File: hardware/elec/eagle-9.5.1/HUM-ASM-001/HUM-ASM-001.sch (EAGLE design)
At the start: 61 parts, among them J1 B2B-XH-AM(LF)(SN), J2 75869-131LF, J22 75869-131LF, J23 75869-131LF, K1 7-1393239-7, K2 7-1393239-7, Q1 IRLB8721PBF, Q2 IRLB8721PBF, U1 MCP23017-E/SP

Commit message: * Fixed crash / recovery inconsistency * Pre silk screen clean up
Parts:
- J10, J11: device MG-Eagle_v1:CON_HEADER_1X4NO_SILK_ALL_ROUND -> MG-Eagle_v1:CON_HEADER_1X4PTH
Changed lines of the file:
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@@
 <part name="U$26" library="MG-Eagle_v1" deviceset="V48" device=""/>
 <part name="U$27" library="MG-Eagle_v1" deviceset="V5.0" device=""/>
-<part name="J10" library="MG-Eagle_v1" deviceset="CON_HEADER_1X4" device="NO_SILK_ALL_ROUND"/>
-<part name="J11" library="MG-Eagle_v1" deviceset="CON_HEADER_1X4" device="NO_SILK_ALL_ROUND"/>
+<part name="J10" library="MG-Eagle_v1" deviceset="CON_HEADER_1X4" device="PTH"/>
+<part name="J11" library="MG-Eagle_v1" deviceset="CON_HEADER_1X4" device="PTH"/>
 <part name="J12" library="MG-Eagle_v1" deviceset="CON_HEADER_1X4" device="NO_SILK_ALL_ROUND"/>
 <part name="U$28" library="MG-Eagle_v1" deviceset="V0_GND" device=""/>

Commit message: * Normalized Text for Names and Values
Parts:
- removed J26, J27: (no value), MG-Eagle_v1:CON_HEADER_1X1-QC_TAB_121786-1
- removed JP13, JP14: CON_JUMPER_PAD-2-NC_BY_TRACE, MG-Eagle_v1:CON_JUMPER_PAD-2-NC_BY_TRACE
- added J5: (no value), MG-Eagle_v1:CON_HEADER_1X7NO_SILK
- added J6: (no value), MG-Eagle_v1:CON_HEADER_1X1-QC_TAB_121786-1
- added JP1, JP2: CON_JUMPER_PAD-2-NC_BY_TRACE, MG-Eagle_v1:CON_JUMPER_PAD-2-NC_BY_TRACE
- added LED2: 3mm Green, MG-Eagle_v1:LED_THT-3MM
- added R11: 100, MG-Eagle_v1:RES_RESISTOR-PTH-1/4W
- ASM-1: value Feather Bluefruit 32u4 -> (none); device MG-Eagle_v1:ASM_ADAFRUIT_FEATHER_BLUEFRUIT -> MG-Eagle_v1:ASM_ADAFRUIT_MAX98306_AMP
- ASM-2: device MG-Eagle_v1:ASM_ADAFRUIT_SOUND_FX_BOARD -> MG-Eagle_v1:ASM_ADAFRUIT_INA169
- ASM-3: value (none) -> Feather Bluefruit 32u4; device MG-Eagle_v1:ASM_ADAFRUIT_MAX98306_AMP -> MG-Eagle_v1:ASM_ADAFRUIT_FEATHER_BLUEFRUIT
- ASM-4: device MG-Eagle_v1:ASM_ADAFRUIT_INA169 -> MG-Eagle_v1:ASM_ADAFRUIT_SOUND_FX_BOARD
- J1: value B2B-XH-AM(LF)(SN) -> (none); device MG-Eagle_v1:CON_JST_2-PIN_B2B-XH-AM -> MG-Eagle_v1:CON_HEADER_1X6NO_SILK_FEMALE_PTH
- J10: device MG-Eagle_v1:CON_HEADER_1X4PTH -> MG-Eagle_v1:CON_HEADER_1X31X03_NO_SILK
- J11: device MG-Eagle_v1:CON_HEADER_1X4PTH -> MG-Eagle_v1:CON_HEADER_1X1-QC_TAB_121786-1
- J12: device MG-Eagle_v1:CON_HEADER_1X4NO_SILK_ALL_ROUND -> MG-Eagle_v1:CON_HEADER_1X12_NO_SILK
- J13: device MG-Eagle_v1:CON_HEADER_1X31X03_NO_SILK -> MG-Eagle_v1:CON_HEADER_1X16-1X16_NO_SILK
- J14: device MG-Eagle_v1:CON_HEADER_1X31X03_NO_SILK -> MG-Eagle_v1:CON_HEADER_1X21X02_NO_SILK
- J15, J16: device MG-Eagle_v1:CON_HEADER_1X21X02_NO_SILK -> MG-Eagle_v1:CON_HEADER_1X14
- J17, J18: device MG-Eagle_v1:CON_HEADER_1X1-QC_TAB_121786-1 -> MG-Eagle_v1:CON_HEADER_1X4PTH
- J19: device MG-Eagle_v1:CON_HEADER_1X5NO_SILK -> MG-Eagle_v1:CON_HEADER_1X21X02_NO_SILK
- J20: value (none) -> 75869-131LF; device MG-Eagle_v1:CON_HEADER_1X21X02_NO_SILK -> MG-Eagle_v1:CON_HEADER_2X3SHROUD
- J21: value (none) -> 75869-131LF; device MG-Eagle_v1:CON_HEADER_1X6NO_SILK_FEMALE_PTH -> MG-Eagle_v1:CON_HEADER_2X3SHROUD
- J22: value 75869-131LF -> (none); device MG-Eagle_v1:CON_HEADER_2X3SHROUD -> MG-Eagle_v1:CON_HEADER_1X4NO_SILK_ALL_ROUND
- J23: value 75869-131LF -> (none); device MG-Eagle_v1:CON_HEADER_2X3SHROUD -> MG-Eagle_v1:CON_HEADER_1X31X03_NO_SILK
- J3: value (none) -> B2B-XH-AM(LF)(SN); device MG-Eagle_v1:CON_HEADER_1X16-1X16_NO_SILK -> MG-Eagle_v1:CON_JST_2-PIN_B2B-XH-AM
- J4: device MG-Eagle_v1:CON_HEADER_1X12_NO_SILK -> MG-Eagle_v1:CON_HEADER_1X21X02_NO_SILK
- J7: device MG-Eagle_v1:CON_HEADER_1X14 -> MG-Eagle_v1:CON_HEADER_1X5NO_SILK
- J8: device MG-Eagle_v1:CON_HEADER_1X14 -> MG-Eagle_v1:CON_HEADER_1X1-QC_TAB_121786-1
- J9: device MG-Eagle_v1:CON_HEADER_1X7NO_SILK -> MG-Eagle_v1:CON_HEADER_1X1-QC_TAB_121786-1
- R1: value 1k -> 10k
- R2: value 100 -> 4k, 1%
- R3: value 10k -> 220
- R5: value 220 -> 100
- R6: value 4k, 1% -> 100
- R7: value 10k -> 1k
- R9: value 100 -> 10k
- VRG-1: value NID100-5 -> LM317; device MG-Eagle_v1:VRG_NID100 -> MG-Eagle_v1:VRG_LM317_TO-220_VERTICAL
- VRG-2: value LM317 -> NID100-5; device MG-Eagle_v1:VRG_LM317_TO-220_VERTICAL -> MG-Eagle_v1:VRG_NID100
- renumbered JP10 to JP4, JP11 to JP5, JP12 to JP6, JP9 to JP3, THM-2 to THM-1
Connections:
- new net N$19: LED2.A, R11.P1
- net !AMP-SHDN: now also ASM-1.!SHTDWN, ASM-3.D10, J12.7, J5.5, R7.P2; no longer ASM-1.D10, ASM-3.!SHTDWN, J4.7, J9.5, R1.P2
- net 24V: now also J3.1, J4.P1, R3.P2, VRG-1.VOUT; no longer J1.1, J20.P1, R5.P2, VRG-2.VOUT
- net 3V: now also ASM-3.3V, J13.2; no longer ASM-1.3V, J3.2
- net 48V: now also J10.P2, J22.3, J22.4, J23.P2, J9.1, VRG-1.VIN, VRG-2.VIN@10, VRG-2.VIN@9; no longer J12.3, J12.4, J13.P2, J14.P2, J26.1, VRG-1.VIN@10, VRG-1.VIN@9, VRG-2.VIN
- net 5V: now also ASM-1.VCC, ASM-2.VCC, ASM-3.USB/VBUS, ASM-4.VIN, J12.3, J14.P1, J15.1, J17.1, J17.2, J17.3, J17.4, J19.P1, J20.1, J20.2, J21.1, J21.2, J5.7, J7.5, LED2.C, VRG-2.VOUT@1, VRG-2.VOUT@2, VRG-2.VOUT@3, VRG-2.VOUT@4; no longer ASM-1.USB/VBUS, ASM-2.VIN, ASM-3.VCC, ASM-4.VCC, J10.1, J10.2, J10.3, J10.4, J15.P1, J16.P1, J19.5, J22.1, J22.2, J23.1, J23.2, J4.3, J8.1, J9.7, VRG-1.VOUT@1, VRG-1.VOUT@2, VRG-1.VOUT@3, VRG-1.VOUT@4
- net ADJ: now also R2.P2, R3.P1, VRG-1.ADJ; no longer R5.P1, R6.P2, VRG-2.ADJ
- net CRNT-MON: now also ASM-2.OUT, ASM-3.A0, J13.5, J7.1; no longer ASM-1.A0, ASM-4.OUT, J19.1, J3.5
- net DFU: now also ASM-3.DFU, J13.16; no longer ASM-1.DFU, J3.16
- net ENCODER-A: now also ASM-3.RX0, J13.14; no longer ASM-1.RX0, J3.14
- net ENCODER-B: now also ASM-3.TX1, J13.15, JP7.1; no longer ASM-1.TX1, J3.15, JP13.1
- net ENCODER-SW: now also ASM-3.A5, J13.10; no longer ASM-1.A5, J3.10
- net FAN-CTRL: now also ASM-3.D6, J12.9, R4.P1; no longer ASM-1.D6, J4.9, R8.P1
- net GND: now also ASM-1.GND, ASM-2.GND, ASM-3.GND@4, ASM-4.GND@14, ASM-4.GND@27, ASM-4.L-GND, ASM-4.R-GND, J13.4, J15.11, J15.14, J15.2, J16.14, J18.2, J18.3, J18.4, J20.5, J20.6, J21.5, J21.6, J5.6, J7.4, J8.1, JP1.1, JP2.1, R1.P2, R11.P2, R2.P1, R7.P1, R9.P2, VRG-2.GND@5, VRG-2.GND@6, VRG-2.GND@7, VRG-2.GND@8; no longer ASM-1.GND@4, ASM-2.GND@14, ASM-2.GND@27, ASM-2.L-GND, ASM-2.R-GND, ASM-3.GND, ASM-4.GND, J11.2, J11.3, J11.4, J19.4, J22.5, J22.6, J23.5, J23.6, J27.1, J3.4, J7.14, J8.11, J8.14, J8.2, J9.6, JP14.1, JP7.1, R1.P1, R3.P2, R6.P1, R7.P2, VRG-1.GND@5, VRG-1.GND@6, VRG-1.GND@7, VRG-1.GND@8
- net I2C-SCL: now also ASM-3.SCL, J12.11; no longer ASM-1.SCL, J4.11
- net I2C-SDA: now also ASM-3.SDA, J12.12; no longer ASM-1.SDA, J4.12
- net K1-NC: now also J10.P1; no longer J13.P1
- net K2-NC: now also J23.P1; no longer J14.P1
- net LED1-DATA: now also ASM-3.D12, J12.5, R5.P2; no longer ASM-1.D12, J4.5, R9.P2
- net LED2-DATA: now also ASM-3.D11, J12.6, R6.P1; no longer ASM-1.D11, J4.6, R10.P1
- net MIST-CTRL: now also ASM-3.D5, J12.10, R8.P1; no longer ASM-1.D5, J4.10, R2.P1
- net MIST-VIN: now also ASM-2.VIN-, J10.P3, J23.P3, J6.1, J7.3; no longer ASM-4.VIN-, J13.P3, J14.P3, J17.1, J19.3
- net N$1: now also ASM-3.!RESET, J13.1; no longer ASM-1.!RESET, J3.1
- net N$10: now also J14.P2, J19.P2, Q2.D, R10.P1; no longer J15.P2, J16.P2, Q1.D, R4.P1
- net N$11: now also Q2.G, R8.P2, R9.P1; no longer Q1.G, R2.P2, R3.P1
- net N$12: now also J3.2, J4.P2, Q1.D; no longer J1.2, J20.P2, Q2.D
- net N$13: now also R10.P2; no longer R4.P2
- net N$14: now also ASM-1.L-IN, J5.3, JP2.2; no longer ASM-3.L-IN, J9.3, JP7.2
- net N$15: now also ASM-1.R-IN, J5.2, JP1.2; no longer ASM-3.R-IN, J9.2, JP8.2
- net N$16: now also ASM-2.VIN+, J7.2; no longer ASM-4.VIN+, J19.2
- net N$17: now also Q1.G, R1.P1, R4.P2; no longer Q2.G, R7.P1, R8.P2
- net N$18: now also J1.1; no longer J21.1
- net N$2: now also ASM-3.AREF, J13.3; no longer ASM-1.AREF, J3.3
- net N$20: now also ASM-3.D9, J12.8; no longer ASM-1.D9, J4.8
- net N$21: now also J1.2; no longer J21.2
- net N$22: now also J1.3; no longer J21.3
- net N$24: now also ASM-3.D13, J12.4; no longer ASM-1.D13, J4.4
- net N$25: now also ASM-3.EN, J12.2; no longer ASM-1.EN, J4.2
- net N$26: now also ASM-4.ACT, J16.13; no longer ASM-2.ACT, J7.13
- net N$27: now also J22.1, VRG-2.R.C.; no longer J12.1, VRG-1.R.C.
- net N$29: now also J22.2, VRG-2.TRIM; no longer J12.2, VRG-1.TRIM
- net N$30: now also ASM-4.TX, J15.5; no longer ASM-2.TX, J8.5
- net N$31: now also ASM-4.RX, J15.6; no longer ASM-2.RX, J8.6
- net N$38: now also ASM-4.UART/GPIO_SEL, J15.7; no longer ASM-2.UART/GPIO_SEL, J8.7
- net N$39: now also J1.4; no longer J21.4
- net N$40: now also J1.5, JP7.2; no longer J21.5, JP13.2
- net N$41: now also J1.6, JP8.2; no longer J21.6, JP14.2
- net N$42: now also J21.3, J21.4, R6.P2; no longer J23.3, J23.4, R10.P2
- net N$5: now also ASM-3.A1, J13.6; no longer ASM-1.A1, J3.6
- net N$6: now also ASM-3.A2, J13.7; no longer ASM-1.A2, J3.7
- net N$7: now also ASM-3.A3, J13.8; no longer ASM-1.A3, J3.8
- net N$8: now also ASM-3.A4, J13.9; no longer ASM-1.A4, J3.9
- net N$9: now also J20.3, J20.4, R5.P1; no longer J22.3, J22.4, R9.P1
- net SFX-0: now also ASM-4.0, J16.2; no longer ASM-2.0, J7.2
- net SFX-1: now also ASM-4.1, J16.3; no longer ASM-2.1, J7.3
- net SFX-10: now also ASM-4.10, J16.12; no longer ASM-2.10, J7.12
- net SFX-2: now also ASM-4.2, J16.4; no longer ASM-2.2, J7.4
- net SFX-3: now also ASM-4.3, J16.5; no longer ASM-2.3, J7.5
- net SFX-4: now also ASM-4.4, J16.6; no longer ASM-2.4, J7.6
- net SFX-5: now also ASM-4.5, J16.7; no longer ASM-2.5, J7.7
- net SFX-6: now also ASM-4.6, J16.8; no longer ASM-2.6, J7.8
- net SFX-7: now also ASM-4.7, J16.9; no longer ASM-2.7, J7.9
- net SFX-8: now also ASM-4.8, J16.10; no longer ASM-2.8, J7.10
- net SFX-9: now also ASM-4.9, J16.11; no longer ASM-2.9, J7.11
- net SFX-LOUT: now also ASM-1.L+IN, ASM-4.L+OUT, J15.13, J5.4; no longer ASM-2.L+OUT, ASM-3.L+IN, J8.13, J9.4
- net SFX-ROUT: now also ASM-1.R+IN, ASM-4.R+OUT, J15.12, J5.1; no longer ASM-2.R+OUT, ASM-3.R+IN, J8.12, J9.1
- net SFX-RST: now also ASM-4.!RESET, J16.1; no longer ASM-2.!RESET, J7.1
- net SFX-VOL-N: now also ASM-4.VOL-, J15.9; no longer ASM-2.VOL-, J8.9
- net SFX-VOL-P: now also ASM-4.VOL+, J15.8; no longer ASM-2.VOL+, J8.8
- net SPI-MISO: now also ASM-3.MISO, J13.13; no longer ASM-1.MISO, J3.13
- net SPI-MOSI: now also ASM-3.MOSI, J13.12; no longer ASM-1.MOSI, J3.12
- net SPI-SCK: now also ASM-3.SCK, J13.11; no longer ASM-1.SCK, J3.11
- net USB/VBUS: now also ASM-4.USB/VBUS, J15.3; no longer ASM-2.USB/VBUS, J8.3
- net VBAT: now also ASM-3.VBAT, J12.1; no longer ASM-1.VBAT, J4.1

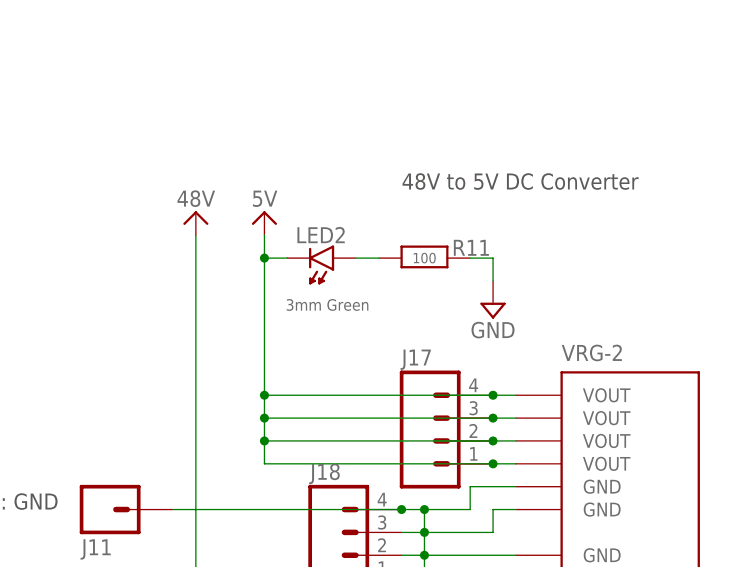
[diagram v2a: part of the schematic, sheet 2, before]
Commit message: * PCB Silk cleanup completed
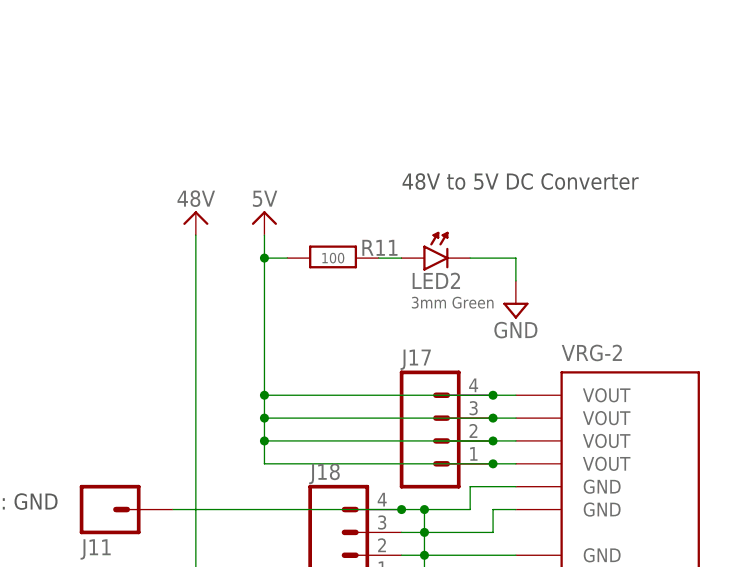
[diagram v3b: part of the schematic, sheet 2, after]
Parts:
- J10, J23: device MG-Eagle_v1:CON_HEADER_1X31X03_NO_SILK -> MG-Eagle_v1:CON_HEADER_1X3PTH
- J2, J20, J21: device MG-Eagle_v1:CON_HEADER_2X3SHROUD -> MG-Eagle_v1:CON_HEADER_2X3-SHROUD
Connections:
- net 5V: now also R11.P1; no longer LED2.C
- net GND: now also LED2.C; no longer R11.P2
- net N$19: now also R11.P2; no longer R11.P1
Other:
- moved on the sheet: LED2, R11
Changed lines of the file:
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@@
 </part>
 <part name="ASM-3" library="MG-Eagle_v1" deviceset="ASM_ADAFRUIT_FEATHER_BLUEFRUIT" device="" value="Feather Bluefruit 32u4"/>
-<part name="J2" library="MG-Eagle_v1" deviceset="CON_HEADER_2X3" device="SHROUD" value="75869-131LF"/>
+<part name="J2" library="MG-Eagle_v1" deviceset="CON_HEADER_2X3" device="-SHROUD" value="75869-131LF"/>
 <part name="U1" library="MG-Eagle_v1" deviceset="IIC_MCP23017-E/SP" device="" value="MCP23017-E/SP"/>
 <part name="FRAME4" library="MG-Eagle_v1" deviceset="SCH_FRAME_LETTER_8.5X11" device="">
@@
 <part name="J22" library="MG-Eagle_v1" deviceset="CON_HEADER_1X4" device="NO_SILK_ALL_ROUND"/>
 <part name="U$28" library="MG-Eagle_v1" deviceset="V0_GND" device=""/>
-<part name="J10" library="MG-Eagle_v1" deviceset="CON_HEADER_1X3" device="1X03_NO_SILK"/>
-<part name="J23" library="MG-Eagle_v1" deviceset="CON_HEADER_1X3" device="1X03_NO_SILK"/>
+<part name="J10" library="MG-Eagle_v1" deviceset="CON_HEADER_1X3" device="PTH"/>
+<part name="J23" library="MG-Eagle_v1" deviceset="CON_HEADER_1X3" device="PTH"/>
 <part name="J19" library="MG-Eagle_v1" deviceset="CON_HEADER_1X2" device="1X02_NO_SILK"/>
 <part name="J14" library="MG-Eagle_v1" deviceset="CON_HEADER_1X2" device="1X02_NO_SILK"/>
@@
 <part name="R5" library="MG-Eagle_v1" deviceset="RES_RESISTOR" device="-PTH-1/4W" value="100"/>
 <part name="R6" library="MG-Eagle_v1" deviceset="RES_RESISTOR" device="-PTH-1/4W" value="100"/>
-<part name="J20" library="MG-Eagle_v1" deviceset="CON_HEADER_2X3" device="SHROUD" value="75869-131LF"/>
-<part name="J21" library="MG-Eagle_v1" deviceset="CON_HEADER_2X3" device="SHROUD" value="75869-131LF"/>
+<part name="J20" library="MG-Eagle_v1" deviceset="CON_HEADER_2X3" device="-SHROUD" value="75869-131LF"/>
+<part name="J21" library="MG-Eagle_v1" deviceset="CON_HEADER_2X3" device="-SHROUD" value="75869-131LF"/>
 <part name="C2" library="MG-Eagle_v1" deviceset="CAP_THT_POL" device="-E-035X080MM" value="100uF, 50V"/>
 <part name="U$36" library="MG-Eagle_v1" deviceset="V0_GND" device=""/>
@@
 <attribute name="NAME" x="180.34" y="-130.302" size="1.778" layer="95" font="vector" rot="MR180"/>
 </instance>
-<instance part="LED2" gate="G$1" x="205.74" y="-99.06" smashed="yes" rot="R180">
-<attribute name="NAME" x="209.804" y="-95.631" size="1.778" layer="95" font="vector" rot="R180"/>
-<attribute name="VALUE" x="212.344" y="-104.902" size="1.27" layer="96" font="vector" ratio="12" rot="R180" align="top-left"/>
-</instance>
-<instance part="R11" gate="G$1" x="218.44" y="-99.06" smashed="yes">
-<attribute name="NAME" x="221.488" y="-98.806" size="1.778" layer="95" font="vector"/>
-<attribute name="VALUE" x="218.44" y="-99.06" size="1.143" layer="96" font="vector" ratio="10" align="center"/>
-</instance>
-<instance part="U$7" gate="G$1" x="226.06" y="-104.14" smashed="yes"/>
+<instance part="LED2" gate="G$1" x="220.98" y="-99.06" smashed="yes">
+<attribute name="NAME" x="216.916" y="-102.489" size="1.778" layer="95" font="vector"/>
+<attribute name="VALUE" x="216.916" y="-103.378" size="1.27" layer="96" font="vector" ratio="12" align="top-left"/>
+</instance>
+<instance part="R11" gate="G$1" x="208.28" y="-99.06" smashed="yes">
+<attribute name="NAME" x="211.328" y="-98.806" size="1.778" layer="95" font="vector"/>
+<attribute name="VALUE" x="208.28" y="-99.06" size="1.143" layer="96" font="vector" ratio="10" align="center"/>
+</instance>
+<instance part="U$7" gate="G$1" x="228.6" y="-104.14" smashed="yes"/>
 </instances>
 <busses>
@@
 </segment>
 <segment>
-<pinref part="R11" gate="G$1" pin="P2"/>
-<wire x1="223.52" y1="-99.06" x2="226.06" y2="-99.06" width="0.1524" layer="91"/>
+<pinref part="LED2" gate="G$1" pin="C"/>
+<wire x1="223.52" y1="-99.06" x2="228.6" y2="-99.06" width="0.1524" layer="91"/>
 <pinref part="U$7" gate="G$1" pin="GND"/>
-<wire x1="226.06" y1="-99.06" x2="226.06" y2="-101.6" width="0.1524" layer="91"/>
+<wire x1="228.6" y1="-99.06" x2="228.6" y2="-101.6" width="0.1524" layer="91"/>
 </segment>
 </net>
@@
 <junction x="226.06" y="-114.3"/>
 <junction x="200.66" y="-114.3"/>
-<pinref part="LED2" gate="G$1" pin="C"/>
+<pinref part="R11" gate="G$1" pin="P1"/>
 <wire x1="203.2" y1="-99.06" x2="200.66" y2="-99.06" width="0.1524" layer="91"/>
 <junction x="200.66" y="-99.06"/>
@@
 <net name="N$19" class="0">
 <segment>
-<pinref part="R11" gate="G$1" pin="P1"/>
+<pinref part="R11" gate="G$1" pin="P2"/>
 <pinref part="LED2" gate="G$1" pin="A"/>
-<wire x1="213.36" y1="-99.06" x2="210.82" y2="-99.06" width="0.1524" layer="91"/>
-</segment>
-</net>
+<wire x1="213.36" y1="-99.06" x2="215.9" y2="-99.06" width="0.1524" layer="91"/>
+</segment>
+</net>
